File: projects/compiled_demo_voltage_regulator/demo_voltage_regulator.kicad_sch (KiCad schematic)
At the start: 7 parts, among them U1 LM7805

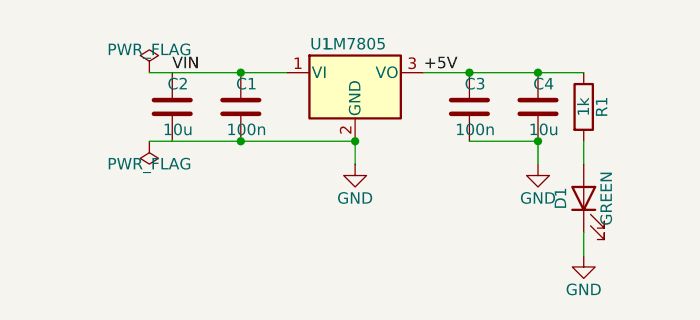
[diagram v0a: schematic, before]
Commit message: F3d+F3e: multi-unit parts and the textplace field autoplacer
Multi-unit: one Symbol per unit (shared ref+lib, distinct unit); nets and
anchors qualify pins as "REF.unit.pin". Resolver targets a specific placed
unit; the geometry probe instantiates per unit. NE5532 (units A/B/C)
compiles first try with both feedback loops wired.

textplace (internal/place2/textplace): deterministic text autoplacement run
at the end of compilation — every visible Reference/Value block is re-placed
horizontally at the least-overlapping side of its body, colliding net labels
flip around their anchor. Fixes the text-collision family the user flagged
on the buck render. KiCad gotcha baked into the pass: a field's drawn angle
is field+symbol rotation, so fields on 90/270 symbols carry a compensating
90 to display horizontal.

All 7 reference circuits now compile from declarative sources with clean
text. Gate demotions (buck SW, ne555 THR/DISCH) are by-design label
fallbacks, zero geometry violations everywhere.

Co-Authored-By: Claude Fable 5 <noreply@anthropic.com>
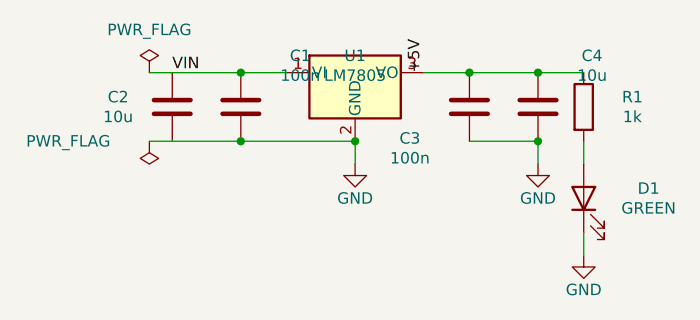
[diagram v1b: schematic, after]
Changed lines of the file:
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@@
     (at 50.8 30.48 0) (unit 1) (exclude_from_sim no) (in_bom yes) (on_board yes) (dnp no)
     (property "Reference" "U1"
-      (at 46.99 27.305 0)
+      (at 50.8 28.6 0)
       (effects
         (font (size 1.27 1.27))))
     (property "Value" "LM7805"
-      (at 50.8 27.305 0)
+      (at 50.8 30.8 0)
       (effects
         (font (size 1.27 1.27))))
@@
     (instances
       (project ""
-        (path "/e33b3df1-013e-4af6-80fe-2b0140d02acf" (reference "U1") (unit 1)))))
+        (path "/48427c94-5b4c-4677-9cda-abd2a168a717" (reference "U1") (unit 1)))))
   (symbol (lib_id "Device:C")
     (at 30.48 34.29 0) (unit 1) (exclude_from_sim no) (in_bom yes) (on_board yes) (dnp no)
     (property "Reference" "C2"
-      (at 31.115 31.75 0)
+      (at 24.47 33.19 0)
       (effects
         (font (size 1.27 1.27))))
     (property "Value" "10u"
-      (at 31.115 36.83 0)
+      (at 24.47 35.39 0)
       (effects
         (font (size 1.27 1.27))))
@@
     (instances
       (project ""
-        (path "/e33b3df1-013e-4af6-80fe-2b0140d02acf" (reference "C2") (unit 1)))))
+        (path "/48427c94-5b4c-4677-9cda-abd2a168a717" (reference "C2") (unit 1)))))
   (symbol (lib_id "Device:C")
     (at 38.1 34.29 0) (unit 1) (exclude_from_sim no) (in_bom yes) (on_board yes) (dnp no)
     (property "Reference" "C1"
-      (at 38.735 31.75 0)
+      (at 44.71 28.6 0)
       (effects
         (font (size 1.27 1.27))))
     (property "Value" "100n"
-      (at 38.735 36.83 0)
+      (at 44.71 30.8 0)
       (effects
         (font (size 1.27 1.27))))
@@
     (instances
       (project ""
-        (path "/e33b3df1-013e-4af6-80fe-2b0140d02acf" (reference "C1") (unit 1)))))
+        (path "/48427c94-5b4c-4677-9cda-abd2a168a717" (reference "C1") (unit 1)))))
   (symbol (lib_id "Device:C")
     (at 63.5 34.29 0) (unit 1) (exclude_from_sim no) (in_bom yes) (on_board yes) (dnp no)
     (property "Reference" "C3"
-      (at 64.135 31.75 0)
+      (at 56.89 37.78 0)
       (effects
         (font (size 1.27 1.27))))
     (property "Value" "100n"
-      (at 64.135 36.83 0)
+      (at 56.89 39.98 0)
       (effects
         (font (size 1.27 1.27))))
@@
     (instances
       (project ""
-        (path "/e33b3df1-013e-4af6-80fe-2b0140d02acf" (reference "C3") (unit 1)))))
+        (path "/48427c94-5b4c-4677-9cda-abd2a168a717" (reference "C3") (unit 1)))))
   (symbol (lib_id "Device:C")
     (at 71.12 34.29 0) (unit 1) (exclude_from_sim no) (in_bom yes) (on_board yes) (dnp no)
     (property "Reference" "C4"
-      (at 71.755 31.75 0)
+      (at 77.13 28.6 0)
       (effects
         (font (size 1.27 1.27))))
     (property "Value" "10u"
-      (at 71.755 36.83 0)
+      (at 77.13 30.8 0)
       (effects
         (font (size 1.27 1.27))))
@@
     (instances
       (project ""
-        (path "/e33b3df1-013e-4af6-80fe-2b0140d02acf" (reference "C4") (unit 1)))))
+        (path "/48427c94-5b4c-4677-9cda-abd2a168a717" (reference "C4") (unit 1)))))
   (symbol (lib_id "Device:R")
     (at 76.2 34.29 0) (unit 1) (exclude_from_sim no) (in_bom yes) (on_board yes) (dnp no)
     (property "Reference" "R1"
-      (at 78.232 34.29 90)
+      (at 81.61 33.19 0)
       (effects
         (font (size 1.27 1.27))))
     (property "Value" "1k"
-      (at 76.2 34.29 90)
+      (at 81.61 35.39 0)
       (effects
         (font (size 1.27 1.27))))
@@
     (instances
       (project ""
-        (path "/e33b3df1-013e-4af6-80fe-2b0140d02acf" (reference "R1") (unit 1)))))
+        (path "/48427c94-5b4c-4677-9cda-abd2a168a717" (reference "R1") (unit 1)))))
   (symbol (lib_id "Device:LED")
     (at 76.2 44.45 90) (unit 1) (exclude_from_sim no) (in_bom yes) (on_board yes) (dnp no)
     (property "Reference" "D1"
-      (at 73.66 44.45 0)
+      (at 83.41 43.35 90)
       (effects
         (font (size 1.27 1.27))))
     (property "Value" "GREEN"
-      (at 78.74 44.45 0)
+      (at 83.41 45.55 90)
       (effects
         (font (size 1.27 1.27))))
@@
     (instances
       (project ""
-        (path "/e33b3df1-013e-4af6-80fe-2b0140d02acf" (reference "D1") (unit 1)))))
+        (path "/48427c94-5b4c-4677-9cda-abd2a168a717" (reference "D1") (unit 1)))))
   (symbol (lib_id "power:GND")
     (at 50.8 40.64 0) (unit 1) (exclude_from_sim no) (in_bom no) (on_board no) (dnp no)
@@
     (instances
       (project ""
-        (path "/e33b3df1-013e-4af6-80fe-2b0140d02acf" (reference "#PWR1") (unit 1)))))
+        (path "/48427c94-5b4c-4677-9cda-abd2a168a717" (reference "#PWR1") (unit 1)))))
   (symbol (lib_id "power:GND")
     (at 71.12 40.64 0) (unit 1) (exclude_from_sim no) (in_bom no) (on_board no) (dnp no)
@@
     (instances
       (project ""
-        (path "/e33b3df1-013e-4af6-80fe-2b0140d02acf" (reference "#PWR2") (unit 1)))))
+        (path "/48427c94-5b4c-4677-9cda-abd2a168a717" (reference "#PWR2") (unit 1)))))
   (symbol (lib_id "power:GND")
     (at 76.2 50.8 0) (unit 1) (exclude_from_sim no) (in_bom no) (on_board no) (dnp no)
@@
     (instances
       (project ""
-        (path "/e33b3df1-013e-4af6-80fe-2b0140d02acf" (reference "#PWR3") (unit 1)))))
+        (path "/48427c94-5b4c-4677-9cda-abd2a168a717" (reference "#PWR3") (unit 1)))))
   (wire
     (pts (xy 30.48 30.48) (xy 38.1 30.48))
@@
     (color 0 0 0 0))
   (label "VIN"
-    (at 30.48 30.48 180) (fields_autoplaced yes)
+    (at 30.48 30.48 0) (fields_autoplaced yes)
     (effects
       (font (size 1.27 1.27)) (justify left bottom))
@@
         (font (size 1.27 1.27)) (hide yes))))
   (label "+5V"
-    (at 58.42 30.48 0) (fields_autoplaced yes)
+    (at 58.42 30.48 90) (fields_autoplaced yes)
     (effects
       (font (size 1.27 1.27)) (justify left bottom))
@@
         (font (size 1.27 1.27)) (hide yes)))
     (property "Value" "PWR_FLAG"
-      (at 27.94 40.64 0)
+      (at 18.93 38.1 0)
       (effects
         (font (size 1.27 1.27))))
@@
     (instances
       (project ""
-        (path "/e33b3df1-013e-4af6-80fe-2b0140d02acf" (reference "#FLG01") (unit 1)))))
+        (path "/48427c94-5b4c-4677-9cda-abd2a168a717" (reference "#FLG01") (unit 1)))))
   (wire
     (pts (xy 30.48 38.1) (xy 27.94 38.1))
@@
         (font (size 1.27 1.27)) (hide yes)))
     (property "Value" "PWR_FLAG"
-      (at 27.94 27.94 0)
+      (at 27.94 25.72 0)
       (effects
         (font (size 1.27 1.27))))
@@
     (instances
       (project ""
-        (path "/e33b3df1-013e-4af6-80fe-2b0140d02acf" (reference "#FLG02") (unit 1)))))
+        (path "/48427c94-5b4c-4677-9cda-abd2a168a717" (reference "#FLG02") (unit 1)))))
   (wire
     (pts (xy 30.48 30.48) (xy 27.94 30.48))

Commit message: F5: human-quality pass — weld, route beauty, silent flags, design guide
The user's mandate: schematics must read as hand-drawn — tidy wires over
tag pairs, clean corners, nothing on screen but symbol, model and value.

- internal/place2/weld: same-net label islands get welded into real wires
  (straight/L/Z) whenever a clean corridor exists; every candidate is
  validated against gate.Check and reverted on any new violation. Redundant
  labels removed, one kept as documentation.
- routeNets beauty policy: a path with more than 3 bends or >70% detour
  over Manhattan distance reads worse than a label — demoted before it is
  ever drawn. Combined with weld this replaces snakes with short wires.
- PWR_FLAG value text hidden (sexp.HidePropertyText): the flag exists for
  ERC, not for the reader.
- design_guide: human-schematic conventions (signal flow, wire-vs-label,
  spacing recipes in grid cells, iteration protocol) distilled from
  SparkFun/KLC/IEEE-315/Altium/H&H research, embedded in the binary and
  served as an MCP tool for authoring LLMs.
- Crystal clusters reworked in both MCU sources: vertical crystal, straight
  XTAL1, single-L XTAL2, horizontal load caps — full Pierce oscillator
  wiring, zero label pairs. NE555 timing chain now fully wired via weld.

Co-Authored-By: Claude Fable 5 <noreply@anthropic.com>
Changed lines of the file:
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@@
     (instances
       (project ""
-        (path "/48427c94-5b4c-4677-9cda-abd2a168a717" (reference "U1") (unit 1)))))
+        (path "/bb503160-f20a-4bd0-a27d-b60941390f3a" (reference "U1") (unit 1)))))
   (symbol (lib_id "Device:C")
     (at 30.48 34.29 0) (unit 1) (exclude_from_sim no) (in_bom yes) (on_board yes) (dnp no)
@@
     (instances
       (project ""
-        (path "/48427c94-5b4c-4677-9cda-abd2a168a717" (reference "C2") (unit 1)))))
+        (path "/bb503160-f20a-4bd0-a27d-b60941390f3a" (reference "C2") (unit 1)))))
   (symbol (lib_id "Device:C")
     (at 38.1 34.29 0) (unit 1) (exclude_from_sim no) (in_bom yes) (on_board yes) (dnp no)
@@
     (instances
       (project ""
-        (path "/48427c94-5b4c-4677-9cda-abd2a168a717" (reference "C1") (unit 1)))))
+        (path "/bb503160-f20a-4bd0-a27d-b60941390f3a" (reference "C1") (unit 1)))))
   (symbol (lib_id "Device:C")
     (at 63.5 34.29 0) (unit 1) (exclude_from_sim no) (in_bom yes) (on_board yes) (dnp no)
@@
     (instances
       (project ""
-        (path "/48427c94-5b4c-4677-9cda-abd2a168a717" (reference "C3") (unit 1)))))
+        (path "/bb503160-f20a-4bd0-a27d-b60941390f3a" (reference "C3") (unit 1)))))
   (symbol (lib_id "Device:C")
     (at 71.12 34.29 0) (unit 1) (exclude_from_sim no) (in_bom yes) (on_board yes) (dnp no)
@@
     (instances
       (project ""
-        (path "/48427c94-5b4c-4677-9cda-abd2a168a717" (reference "C4") (unit 1)))))
+        (path "/bb503160-f20a-4bd0-a27d-b60941390f3a" (reference "C4") (unit 1)))))
   (symbol (lib_id "Device:R")
     (at 76.2 34.29 0) (unit 1) (exclude_from_sim no) (in_bom yes) (on_board yes) (dnp no)
@@
     (instances
       (project ""
-        (path "/48427c94-5b4c-4677-9cda-abd2a168a717" (reference "R1") (unit 1)))))
+        (path "/bb503160-f20a-4bd0-a27d-b60941390f3a" (reference "R1") (unit 1)))))
   (symbol (lib_id "Device:LED")
     (at 76.2 44.45 90) (unit 1) (exclude_from_sim no) (in_bom yes) (on_board yes) (dnp no)
@@
     (instances
       (project ""
-        (path "/48427c94-5b4c-4677-9cda-abd2a168a717" (reference "D1") (unit 1)))))
+        (path "/bb503160-f20a-4bd0-a27d-b60941390f3a" (reference "D1") (unit 1)))))
   (symbol (lib_id "power:GND")
     (at 50.8 40.64 0) (unit 1) (exclude_from_sim no) (in_bom no) (on_board no) (dnp no)
@@
     (instances
       (project ""
-        (path "/48427c94-5b4c-4677-9cda-abd2a168a717" (reference "#PWR1") (unit 1)))))
+        (path "/bb503160-f20a-4bd0-a27d-b60941390f3a" (reference "#PWR1") (unit 1)))))
   (symbol (lib_id "power:GND")
     (at 71.12 40.64 0) (unit 1) (exclude_from_sim no) (in_bom no) (on_board no) (dnp no)
@@
     (instances
       (project ""
-        (path "/48427c94-5b4c-4677-9cda-abd2a168a717" (reference "#PWR2") (unit 1)))))
+        (path "/bb503160-f20a-4bd0-a27d-b60941390f3a" (reference "#PWR2") (unit 1)))))
   (symbol (lib_id "power:GND")
     (at 76.2 50.8 0) (unit 1) (exclude_from_sim no) (in_bom no) (on_board no) (dnp no)
@@
     (instances
       (project ""
-        (path "/48427c94-5b4c-4677-9cda-abd2a168a717" (reference "#PWR3") (unit 1)))))
+        (path "/bb503160-f20a-4bd0-a27d-b60941390f3a" (reference "#PWR3") (unit 1)))))
   (wire
     (pts (xy 30.48 30.48) (xy 38.1 30.48))
@@
         (font (size 1.27 1.27)) (hide yes)))
     (property "Value" "PWR_FLAG"
-      (at 18.93 38.1 0)
-      (effects
-        (font (size 1.27 1.27))))
+      (at 27.94 40.64 0)
+      (effects
+        (font (size 1.27 1.27)) (hide yes)))
     (property "Footprint" ""
       (at 27.94 38.1 0)
@@
     (instances
       (project ""
-        (path "/48427c94-5b4c-4677-9cda-abd2a168a717" (reference "#FLG01") (unit 1)))))
+        (path "/bb503160-f20a-4bd0-a27d-b60941390f3a" (reference "#FLG01") (unit 1)))))
   (wire
     (pts (xy 30.48 38.1) (xy 27.94 38.1))
@@
         (font (size 1.27 1.27)) (hide yes)))
     (property "Value" "PWR_FLAG"
-      (at 27.94 25.72 0)
-      (effects
-        (font (size 1.27 1.27))))
+      (at 27.94 27.94 0)
+      (effects
+        (font (size 1.27 1.27)) (hide yes)))
     (property "Footprint" ""
       (at 27.94 30.48 0)
@@
     (instances
       (project ""
-        (path "/48427c94-5b4c-4677-9cda-abd2a168a717" (reference "#FLG02") (unit 1)))))
+        (path "/bb503160-f20a-4bd0-a27d-b60941390f3a" (reference "#FLG02") (unit 1)))))
   (wire
     (pts (xy 30.48 30.48) (xy 27.94 30.48))

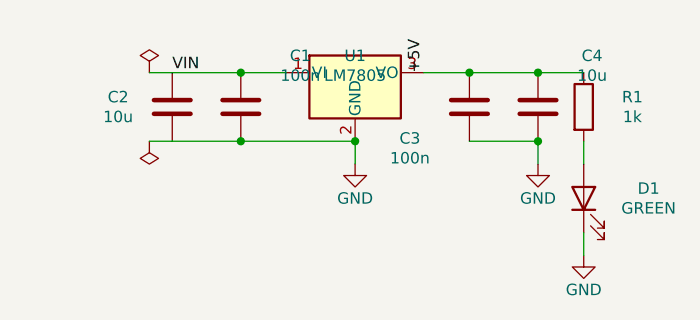
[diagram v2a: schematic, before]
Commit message: Body model sees real symbol graphics; quiet nets drop junction tags
User-reported flaws from visual review, both fixed at the root:

- Wires over symbol artwork: the body model was pin-derived and blind to
  drawn graphics — an op-amp triangle's vertices stick out beyond the pin
  box, so "legal" wires crossed the drawing. internal/sexp/graphics.go now
  parses rectangle/polyline/circle/arc/bezier extents per unit with the
  exact pin transform; metrics.BodyBBox unions them with the legacy box,
  clamped off pin tips (Device:LED's emission arrows overhang the cathode
  pin and would have swallowed it). NE5532 feedback: 8 stroke crossings
  through the triangle before, 0 after (loops now label pairs). The model
  also exposed genuinely bad baked geometry in mcu_minimal_atmega328's
  crystal — repositioned with the template contract intact.

- "ANODE" tag on a resistor leg: net names with a "_" prefix are now
  quiet — connectivity only, their documentation label is stripped at the
  end of compilation when the wiring alone keeps the net whole. Junction
  nodes (R->LED) stay unlabeled like in any hand-drawn schematic.

- Battery hump: led_18650 anchors R1 in the pin's exit direction; the
  design guide gains the "respect the pin's exit direction" and "internal
  junctions carry no tag" recipes.

Co-Authored-By: Claude Fable 5 <noreply@anthropic.com>
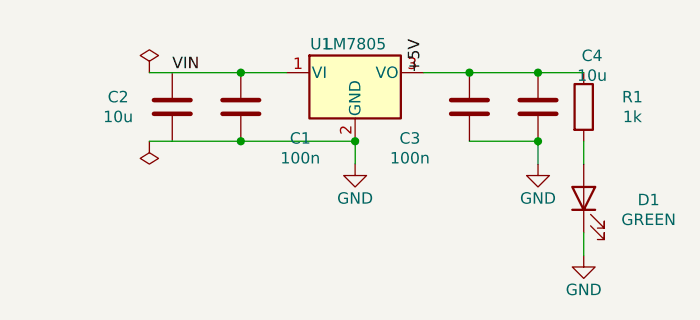
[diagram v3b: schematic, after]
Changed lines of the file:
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@@
     (at 50.8 30.48 0) (unit 1) (exclude_from_sim no) (in_bom yes) (on_board yes) (dnp no)
     (property "Reference" "U1"
-      (at 50.8 28.6 0)
+      (at 46.99 27.305 0)
       (effects
         (font (size 1.27 1.27))))
     (property "Value" "LM7805"
-      (at 50.8 30.8 0)
+      (at 50.8 27.305 0)
       (effects
         (font (size 1.27 1.27))))
@@
     (instances
       (project ""
-        (path "/bb503160-f20a-4bd0-a27d-b60941390f3a" (reference "U1") (unit 1)))))
+        (path "/d8168266-f8e7-40a9-ad0f-924c5b7b36c0" (reference "U1") (unit 1)))))
   (symbol (lib_id "Device:C")
     (at 30.48 34.29 0) (unit 1) (exclude_from_sim no) (in_bom yes) (on_board yes) (dnp no)
@@
     (instances
       (project ""
-        (path "/bb503160-f20a-4bd0-a27d-b60941390f3a" (reference "C2") (unit 1)))))
+        (path "/d8168266-f8e7-40a9-ad0f-924c5b7b36c0" (reference "C2") (unit 1)))))
   (symbol (lib_id "Device:C")
     (at 38.1 34.29 0) (unit 1) (exclude_from_sim no) (in_bom yes) (on_board yes) (dnp no)
     (property "Reference" "C1"
-      (at 44.71 28.6 0)
+      (at 44.71 37.78 0)
       (effects
         (font (size 1.27 1.27))))
     (property "Value" "100n"
-      (at 44.71 30.8 0)
+      (at 44.71 39.98 0)
       (effects
         (font (size 1.27 1.27))))
@@
     (instances
       (project ""
-        (path "/bb503160-f20a-4bd0-a27d-b60941390f3a" (reference "C1") (unit 1)))))
+        (path "/d8168266-f8e7-40a9-ad0f-924c5b7b36c0" (reference "C1") (unit 1)))))
   (symbol (lib_id "Device:C")
     (at 63.5 34.29 0) (unit 1) (exclude_from_sim no) (in_bom yes) (on_board yes) (dnp no)
@@
     (instances
       (project ""
-        (path "/bb503160-f20a-4bd0-a27d-b60941390f3a" (reference "C3") (unit 1)))))
+        (path "/d8168266-f8e7-40a9-ad0f-924c5b7b36c0" (reference "C3") (unit 1)))))
   (symbol (lib_id "Device:C")
     (at 71.12 34.29 0) (unit 1) (exclude_from_sim no) (in_bom yes) (on_board yes) (dnp no)
@@
     (instances
       (project ""
-        (path "/bb503160-f20a-4bd0-a27d-b60941390f3a" (reference "C4") (unit 1)))))
+        (path "/d8168266-f8e7-40a9-ad0f-924c5b7b36c0" (reference "C4") (unit 1)))))
   (symbol (lib_id "Device:R")
     (at 76.2 34.29 0) (unit 1) (exclude_from_sim no) (in_bom yes) (on_board yes) (dnp no)
@@
     (instances
       (project ""
-        (path "/bb503160-f20a-4bd0-a27d-b60941390f3a" (reference "R1") (unit 1)))))
+        (path "/d8168266-f8e7-40a9-ad0f-924c5b7b36c0" (reference "R1") (unit 1)))))
   (symbol (lib_id "Device:LED")
     (at 76.2 44.45 90) (unit 1) (exclude_from_sim no) (in_bom yes) (on_board yes) (dnp no)
     (property "Reference" "D1"
-      (at 83.41 43.35 90)
+      (at 83.41 44.62 90)
       (effects
         (font (size 1.27 1.27))))
     (property "Value" "GREEN"
-      (at 83.41 45.55 90)
+      (at 83.41 46.82 90)
       (effects
         (font (size 1.27 1.27))))
@@
     (instances
       (project ""
-        (path "/bb503160-f20a-4bd0-a27d-b60941390f3a" (reference "D1") (unit 1)))))
+        (path "/d8168266-f8e7-40a9-ad0f-924c5b7b36c0" (reference "D1") (unit 1)))))
   (symbol (lib_id "power:GND")
     (at 50.8 40.64 0) (unit 1) (exclude_from_sim no) (in_bom no) (on_board no) (dnp no)
@@
     (instances
       (project ""
-        (path "/bb503160-f20a-4bd0-a27d-b60941390f3a" (reference "#PWR1") (unit 1)))))
+        (path "/d8168266-f8e7-40a9-ad0f-924c5b7b36c0" (reference "#PWR1") (unit 1)))))
   (symbol (lib_id "power:GND")
     (at 71.12 40.64 0) (unit 1) (exclude_from_sim no) (in_bom no) (on_board no) (dnp no)
@@
     (instances
       (project ""
-        (path "/bb503160-f20a-4bd0-a27d-b60941390f3a" (reference "#PWR2") (unit 1)))))
+        (path "/d8168266-f8e7-40a9-ad0f-924c5b7b36c0" (reference "#PWR2") (unit 1)))))
   (symbol (lib_id "power:GND")
     (at 76.2 50.8 0) (unit 1) (exclude_from_sim no) (in_bom no) (on_board no) (dnp no)
@@
     (instances
       (project ""
-        (path "/bb503160-f20a-4bd0-a27d-b60941390f3a" (reference "#PWR3") (unit 1)))))
+        (path "/d8168266-f8e7-40a9-ad0f-924c5b7b36c0" (reference "#PWR3") (unit 1)))))
   (wire
     (pts (xy 30.48 30.48) (xy 38.1 30.48))
@@
     (instances
       (project ""
-        (path "/bb503160-f20a-4bd0-a27d-b60941390f3a" (reference "#FLG01") (unit 1)))))
+        (path "/d8168266-f8e7-40a9-ad0f-924c5b7b36c0" (reference "#FLG01") (unit 1)))))
   (wire
     (pts (xy 30.48 38.1) (xy 27.94 38.1))
@@
     (instances
       (project ""
-        (path "/bb503160-f20a-4bd0-a27d-b60941390f3a" (reference "#FLG02") (unit 1)))))
+        (path "/d8168266-f8e7-40a9-ad0f-924c5b7b36c0" (reference "#FLG02") (unit 1)))))
   (wire
     (pts (xy 30.48 30.48) (xy 27.94 30.48))
